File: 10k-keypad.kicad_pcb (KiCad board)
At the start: 2 copper layers, 62 parts, among them J1 AVR-ISP-6, K1 SW_Push, K10 SW_Push, K2 SW_Push, K3 SW_Push, K4 SW_Push, K5 SW_Push, K6 SW_Push, K7 SW_Push, K8 SW_Push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

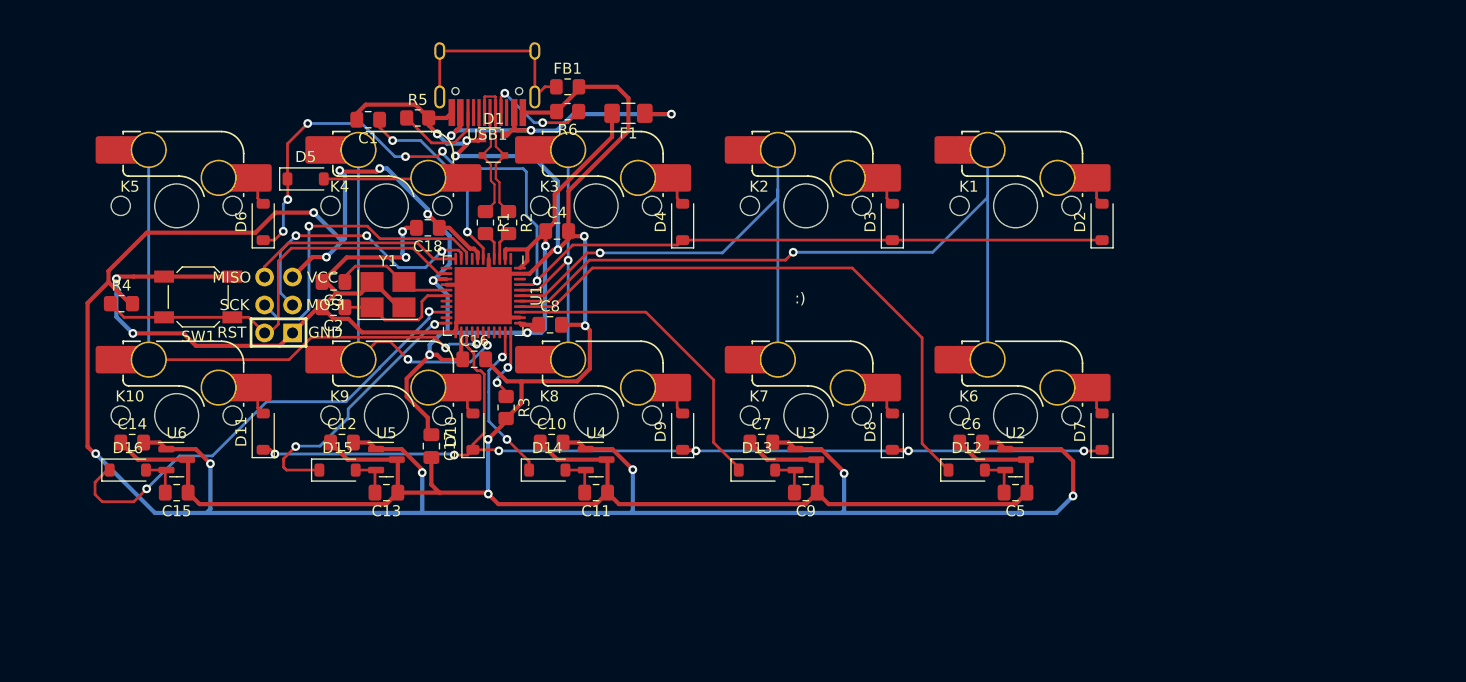
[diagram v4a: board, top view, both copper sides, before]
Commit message: new board edge
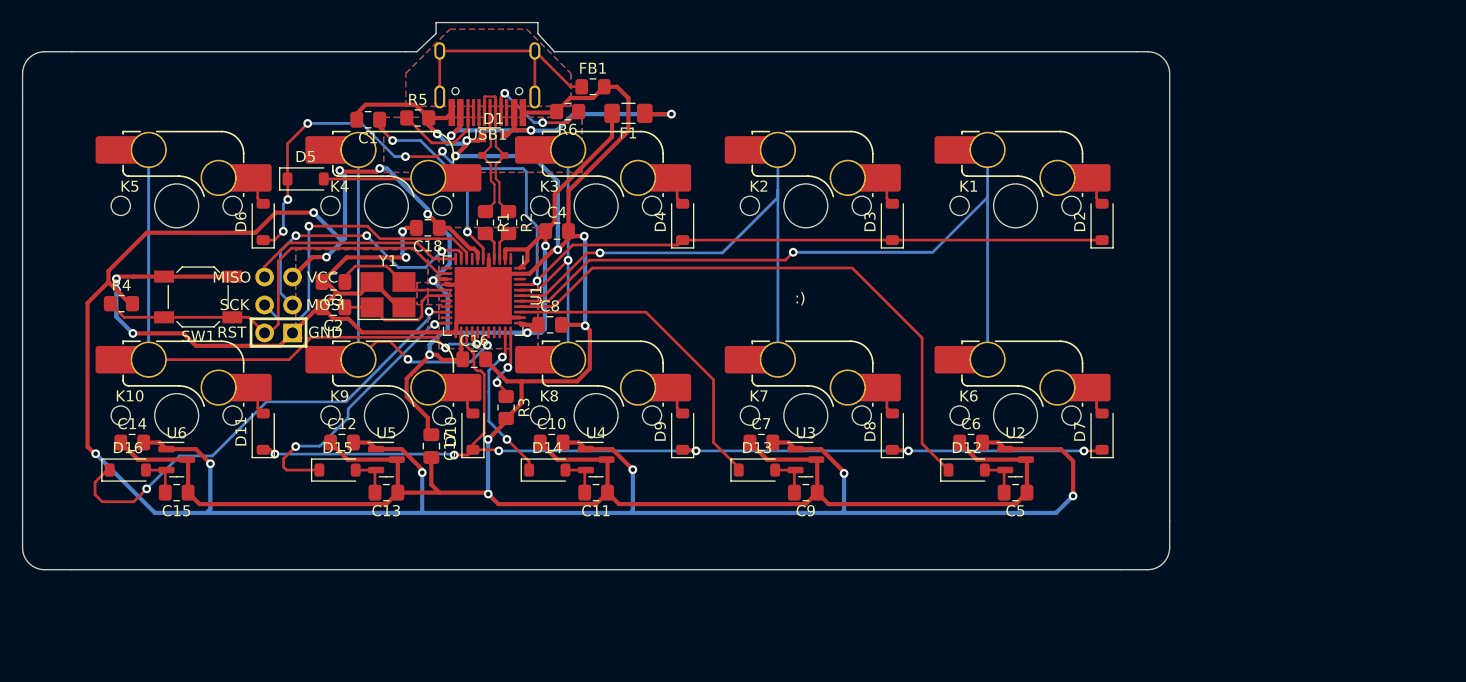
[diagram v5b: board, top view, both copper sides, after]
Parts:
- moved FB1 2.30 mm to (132.0, 42.2)
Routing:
- net Earth: track 19.3 -> 22.8 mm
- added copper zone on B.Cu, net Earth
- added copper zone on F.Cu, net Earth
- added copper zone on B.Cu, net GND
- added copper zone on F.Cu, net GND
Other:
- board outline added: 104.2 x 49.7 mm

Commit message: fix ground fill
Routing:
- net GND: track 335.8 -> 335.9 mm, vias 12 -> 14
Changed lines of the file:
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@@
   (segment (start 165.31 74.535) (end 166.86 76.085) (width 0.381) (layer "F.Cu") (net 2))
   (segment (start 120.537802 47.107802) (end 120.537802 47.472198) (width 0.381) (layer "F.Cu") (net 2))
+  (segment (start 122 61.16) (end 122 61) (width 0.381) (layer "F.Cu") (net 2))
   (segment (start 133.3225 79.085) (end 134.368 80.1305) (width 0.381) (layer "F.Cu") (net 2))
   (segment (start 151.327 80.1305) (end 152.3725 79.085) (width 0.381) (layer "F.Cu") (net 2))
@@
   (segment (start 115.0355 55.03) (end 114.7 55.3655) (width 0.381) (layer "F.Cu") (net 2))
   (segment (start 124.183 68.9755) (end 125.51 68.9755) (width 0.381) (layer "F.Cu") (net 2))
-  (segment (start 109.6225 57.72) (end 107.3925 59.95) (width 0.381) (layer "F.Cu") (net 2))
   (segment (start 107.3925 62.25) (end 108.438 63.2955) (width 0.381) (layer "F.Cu") (net 2))
   (segment (start 111.35 43.84) (end 115.87 43.84) (width 0.381) (layer "F.Cu") (net 2))
@@
   (segment (start 88.91 59.46) (end 88.71 59.66) (width 0.381) (layer "F.Cu") (net 2))
   (segment (start 122.365 79.085) (end 118.05 79.085) (width 0.381) (layer "F.Cu") (net 2))
-  (segment (start 115.02 57.72) (end 109.6225 57.72) (width 0.381) (layer "F.Cu") (net 2))
+  (segment (start 122 61) (end 121.84 61) (width 0.381) (layer "F.Cu") (net 2))
   (segment (start 147.81 76.085) (end 152.2725 76.085) (width 0.381) (layer "F.Cu") (net 2))
   (segment (start 166.86 76.085) (end 171.3225 76.085) (width 0.381) (layer "F.Cu") (net 2))
+  (segment (start 109.6225 57.72) (end 107.3925 59.95) (width 0.381) (layer "F.Cu") (net 2))
   (segment (start 120.537802 47.472198) (end 119.5 48.51) (width 0.381) (layer "F.Cu") (net 2))
   (segment (start 153.418 80.1305) (end 170.377 80.1305) (width 0.381) (layer "F.Cu") (net 2))
   (segment (start 122.49 79.21) (end 122.365 79.085) (width 0.381) (layer "F.Cu") (net 2))
   (segment (start 131.21 55.79) (end 130.2375 55.79) (width 0.381) (layer "F.Cu") (net 2))
+  (segment (start 121.84 61) (end 121.03 60.19) (width 0.381) (layer "F.Cu") (net 2))
+  (segment (start 115.02 57.72) (end 109.6225 57.72) (width 0.381) (layer "F.Cu") (net 2))
   (segment (start 95.2225 79.085) (end 95.2225 76.185) (width 0.381) (layer "F.Cu") (net 2))
   (segment (start 115.9625 55.03) (end 115.0355 55.03) (width 0.381) (layer "F.Cu") (net 2))
@@
   (segment (start 114.2725 79.085) (end 114.2725 76.185) (width 0.381) (layer "F.Cu") (net 2))
   (segment (start 128.76 76.085) (end 133.2225 76.085) (width 0.381) (layer "F.Cu") (net 2))
-  (segment (start 122.03 61.19) (end 121.03 60.19) (width 0.381) (layer "F.Cu") (net 2))
+  (segment (start 122.03 61.19) (end 122 61.16) (width 0.381) (layer "F.Cu") (net 2))
   (segment (start 134.368 80.1305) (end 151.327 80.1305) (width 0.381) (layer "F.Cu") (net 2))
   (segment (start 122.49 79.21) (end 123.4105 80.1305) (width 0.381) (layer "F.Cu") (net 2))
@@
   (via (at 122.47 74.25) (size 0.8) (drill 0.4) (layers "F.Cu" "B.Cu") (net 2))
   (via (at 88.71 59.66) (size 0.8) (drill 0.4) (layers "F.Cu" "B.Cu") (net 2))
+  (via (at 111.75 57.72) (size 0.8) (drill 0.4) (layers "F.Cu" "B.Cu") (net 2))
   (via (at 131.29 63.93) (size 0.8) (drill 0.4) (layers "F.Cu" "B.Cu") (net 2))
   (via (at 122.49 79.21) (size 0.8) (drill 0.4) (layers "F.Cu" "B.Cu") (net 2))
+  (via (at 122.03 61.19) (size 0.8) (drill 0.4) (layers "F.Cu" "B.Cu") (net 2))
   (via (at 117.86 46.5) (size 0.8) (drill 0.4) (layers "F.Cu" "B.Cu") (net 2))
   (via (at 120.537802 47.107802) (size 0.8) (drill 0.4) (layers "F.Cu" "B.Cu") (net 2))

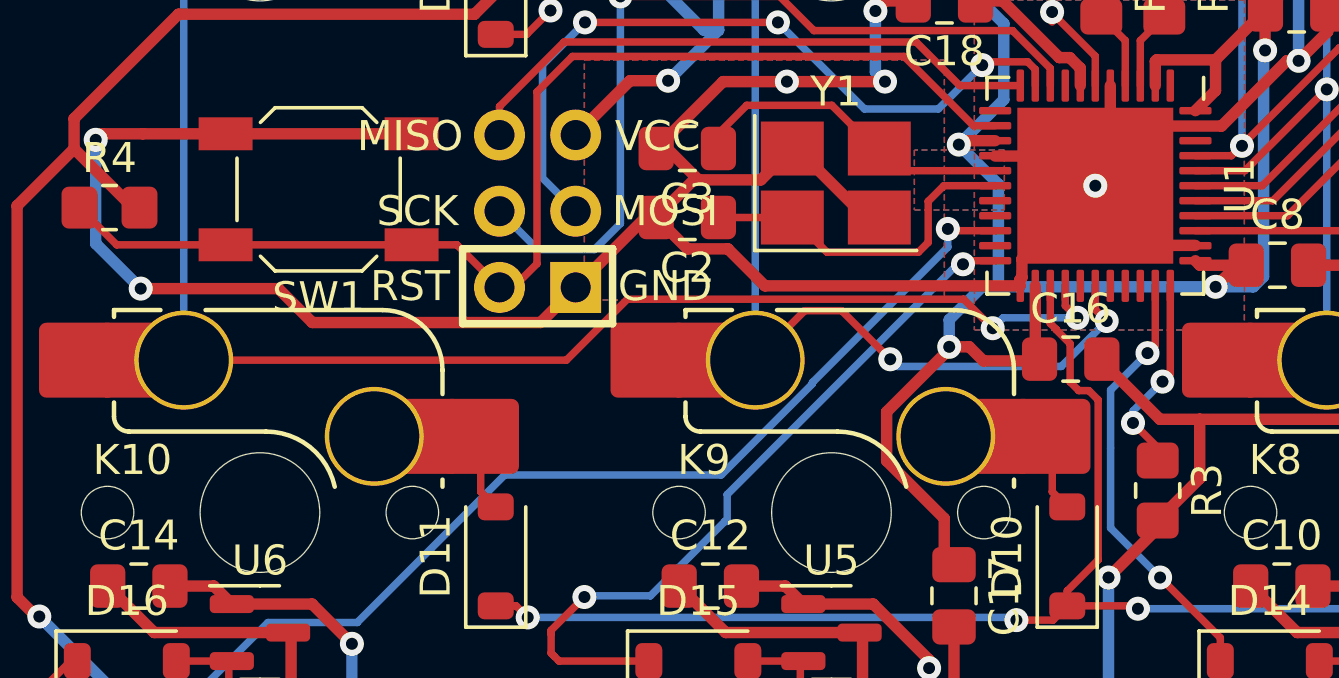
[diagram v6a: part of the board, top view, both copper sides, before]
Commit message: correct analog pins
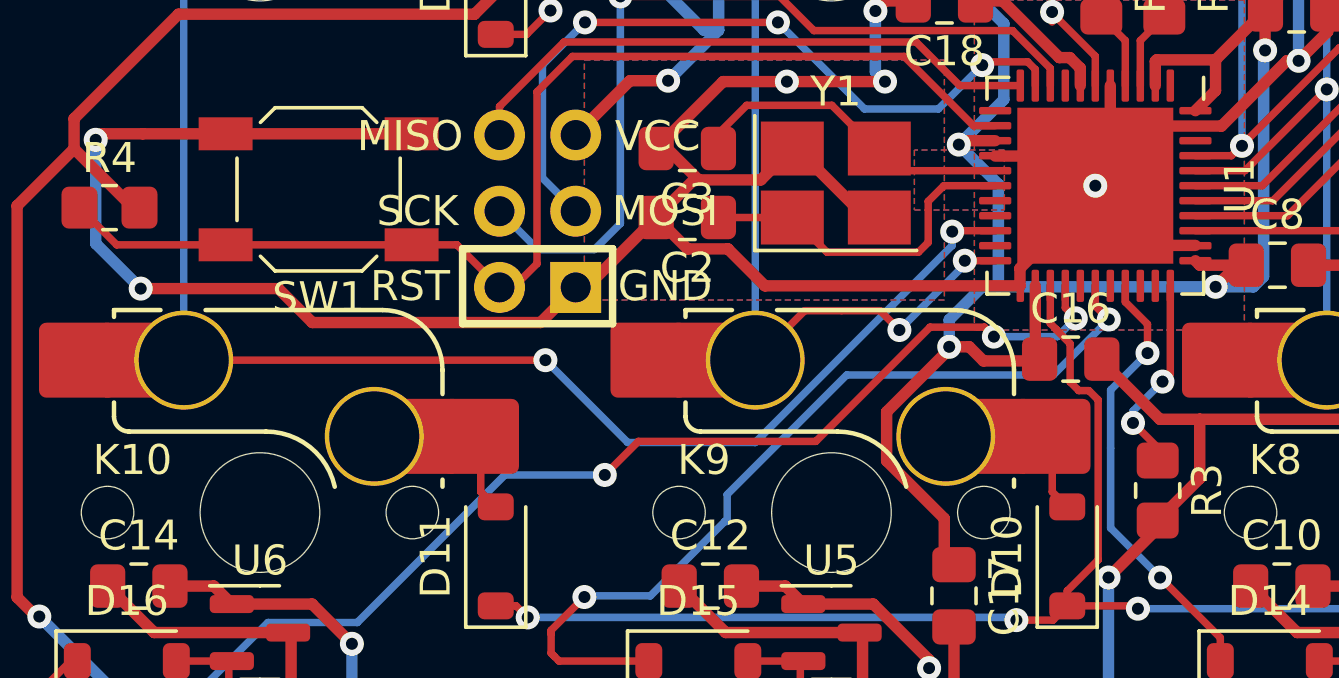
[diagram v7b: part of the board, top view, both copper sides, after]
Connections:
- U1 pad 20: HALL5 -> COL5
- U1 pad 22: HALL4 -> COL4
- U1 pad 26: COL5 -> HALL5
- U1 pad 28: COL4 -> HALL4
- U1 pad 30: unconnected-(U1-PB6-Pad30) -> HALL3
- U1 pad 32: HALL3 -> unconnected-(U1-PC7-Pad32)
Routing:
- net COL4: track 34.2 -> 29.0 mm
- net HALL4: track 24.6 -> 28.8 mm
- net HALL5: track 42.7 -> 45.2 mm, vias 2 -> 4
- net COL5: track 51.5 -> 50.4 mm

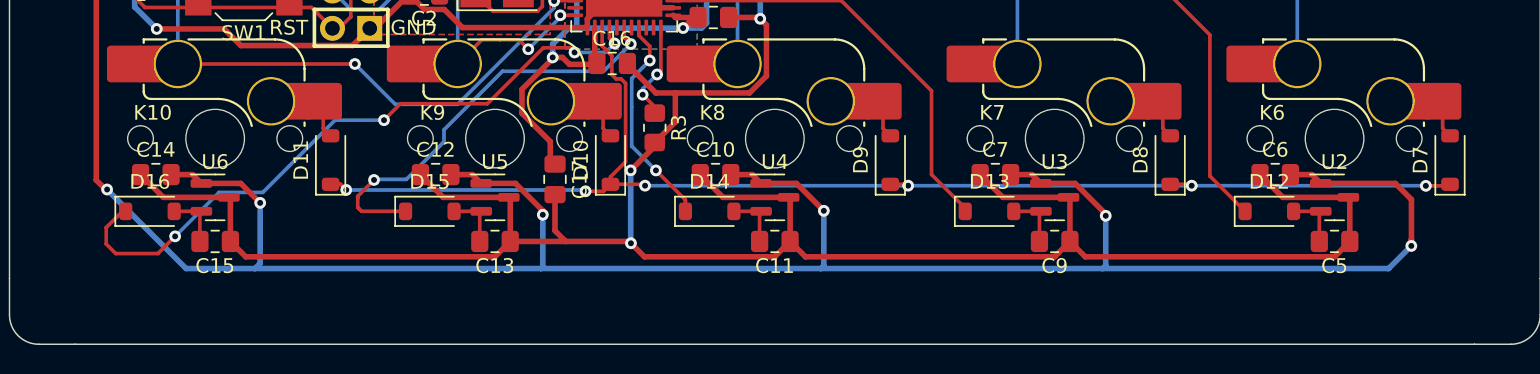
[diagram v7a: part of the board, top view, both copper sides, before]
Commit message: move hall sensors to center
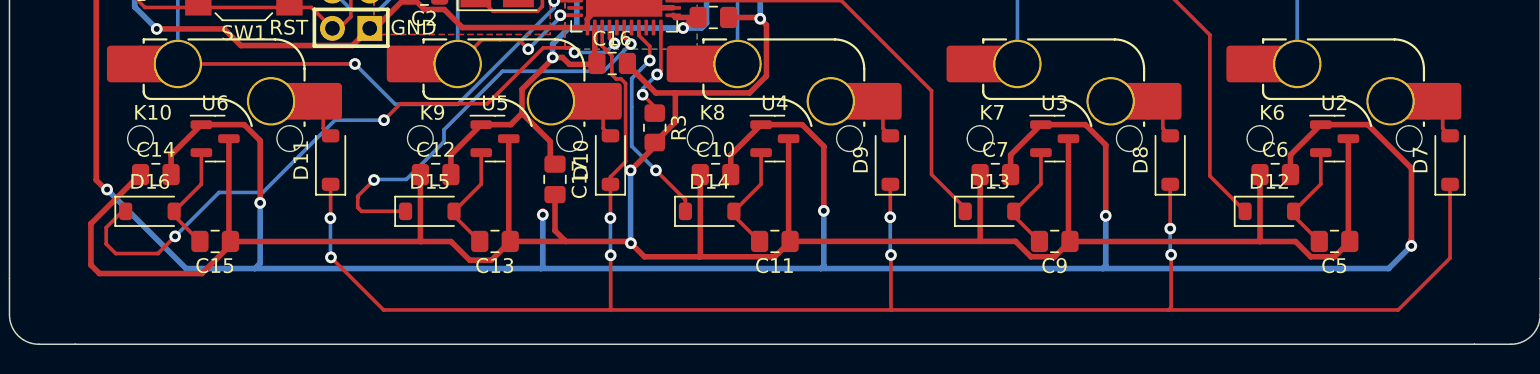
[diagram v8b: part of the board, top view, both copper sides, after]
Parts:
- K10, K6, K7, K8, K9: footprint marbastlib-mx:SW_MX_HS_CPG151101S11_1u -> custom:SW_MX_HS_CPG151101S11_1u_no_center
- moved U2 4.00 mm to (170.4, 72.1)
- moved U3 4.00 mm to (151.3, 72.1)
- moved U4 4.00 mm to (132.3, 72.1)
- moved U5 4.00 mm to (113.2, 72.1)
- moved U6 4.00 mm to (94.2, 72.1)
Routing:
- net ROW2: track 91.4 -> 127.1 mm, vias 6 -> 8
- net GND: track 336.2 -> 360.8 mm
- net +5V: track 296.8 -> 320.3 mm
- net Net-(D15-A): track 3.94 -> 7.54 mm
- net Net-(D14-A): track 3.94 -> 7.54 mm
- net Net-(D13-A): track 3.94 -> 7.54 mm
- net Net-(D12-A): track 3.94 -> 7.54 mm
- net Net-(D16-A): track 3.94 -> 7.54 mm
